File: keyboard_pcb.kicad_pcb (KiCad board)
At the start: 2 copper layers, 436.2 x 123.8 mm, 214 parts, among them J1 Conn_01x04_Female, J2 , J3 Conn_01x03_Male, SW1 SW_Push, SW10 SW_Push, SW100 SW_Push, SW101 SW_Push, SW102 SW_Push, SW103 SW_Push, SW104 SW_Push, SW105 SW_Push, SW11 SW_Push, SW12 SW_Push, SW13 SW_Push, SW14 SW_Push, SW15 SW_Push, SW16 SW_Push, SW17 SW_Push, SW18 SW_Push, SW19 SW_Push, SW2 SW_Push, SW20 SW_Push, SW21 SW_Push, SW22 SW_Push, SW23 SW_Push, SW24 SW_Push, SW25 SW_Push, SW26 SW_Push, SW27 SW_Push, SW28 SW_Push, SW29 SW_Push, SW3 SW_Push, SW30 SW_Push, SW31 SW_Push, SW32 SW_Push, SW33 SW_Push, SW34 SW_Push, SW35 SW_Push, SW36 SW_Push, SW37 SW_Push, SW38 SW_Push, SW39 SW_Push, SW4 SW_Push, SW40 SW_Push, SW41 SW_Push, SW42 SW_Push, SW43 SW_Push, SW44 SW_Push, SW45 SW_Push, SW46 SW_Push, SW47 SW_Push, SW48 SW_Push, SW49 SW_Push, SW5 SW_Push, SW50 SW_Push, SW51 SW_Push, SW52 SW_Push, SW53 SW_Push, SW54 SW_Push, SW55 SW_Push, SW56 SW_Push, SW57 SW_Push, SW58 SW_Push, SW59 SW_Push, SW6 SW_Push, SW60 SW_Push, SW61 SW_Push, SW62 SW_Push, SW63 SW_Push, SW64 SW_Push, SW65 SW_Push, SW66 SW_Push, SW67 SW_Push, SW68 SW_Push, SW69 SW_Push, SW7 SW_Push, SW70 SW_Push, SW71 SW_Push, SW72 SW_Push, SW73 SW_Push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

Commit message: Fixed missing connections and schematic changes
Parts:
- added J4: Conn_01x04_Female, Connector_PinHeader_2.54mm:PinHeader_1x04_P2.54mm_Vertical, F.Cu at (407.0, 19.7)
- moved J3 7.18 mm to (414.7, 14.6), turned to 180 degrees
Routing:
- net ROW4: track 243.8 -> 460.5 mm
- net SDA: track 25.2 -> 39.9 mm
- net 3V3: track 23.7 -> 9.72 mm
- net SCL: track 20.4 -> 32.7 mm
- net 5V: track 36.4 -> 38.5 mm
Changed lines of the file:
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@@
     (thickness 1.6)
     (drawings 8)
-    (tracks 454)
+    (tracks 458)
     (zones 0)
-    (modules 214)
+    (modules 215)
     (nets 146)
   )
@@
     (add_net GND)
   )
+  (module Connector_PinHeader_2.54mm:PinHeader_1x04_P2.54mm_Vertical (layer Front)
+    (at 407.035 19.685 90)
+    (descr "Through hole straight pin header, 1x04, 2.54mm pitch, single row")
+    (tags "Through hole pin header THT 1x04 2.54mm single row")
+    (fp_text reference J4 (at 0 -2.33 90) (layer F.SilkS)
+      (effects (font (size 1 1) (thickness 0.15)))
+    )
+    (fp_text value Conn_01x04_Female (at 0 9.95 90) (layer F.Fab)
+      (effects (font (size 1 1) (thickness 0.15)))
+    )
+    (fp_text user %R (at 0 3.81) (layer F.Fab)
+      (effects (font (size 1 1) (thickness 0.15)))
+    )
+    (fp_line (start -0.635 -1.27) (end 1.27 -1.27) (layer F.Fab) (width 0.1))
+    (fp_line (start 1.27 -1.27) (end 1.27 8.89) (layer F.Fab) (width 0.1))
+    (fp_line (start 1.27 8.89) (end -1.27 8.89) (layer F.Fab) (width 0.1))
+    (fp_line (start -1.27 8.89) (end -1.27 -0.635) (layer F.Fab) (width 0.1))
+    (fp_line (start -1.27 -0.635) (end -0.635 -1.27) (layer F.Fab) (width 0.1))
+    (fp_line (start -1.33 8.95) (end 1.33 8.95) (layer F.SilkS) (width 0.12))
+    (fp_line (start -1.33 1.27) (end -1.33 8.95) (layer F.SilkS) (width 0.12))
+    (fp_line (start 1.33 1.27) (end 1.33 8.95) (layer F.SilkS) (width 0.12))
+    (fp_line (start -1.33 1.27) (end 1.33 1.27) (layer F.SilkS) (width 0.12))
+    (fp_line (start -1.33 0) (end -1.33 -1.33) (layer F.SilkS) (width 0.12))
+    (fp_line (start -1.33 -1.33) (end 0 -1.33) (layer F.SilkS) (width 0.12))
+    (fp_line (start -1.8 -1.8) (end -1.8 9.4) (layer F.CrtYd) (width 0.05))
+    (fp_line (start -1.8 9.4) (end 1.8 9.4) (layer F.CrtYd) (width 0.05))
+    (fp_line (start 1.8 9.4) (end 1.8 -1.8) (layer F.CrtYd) (width 0.05))
+    (fp_line (start 1.8 -1.8) (end -1.8 -1.8) (layer F.CrtYd) (width 0.05))
+    (pad 4 thru_hole oval (at 0 7.62 90) (size 1.7 1.7) (drill 1) (layers *.Cu *.Mask)
+      (net 138 3V3))
+    (pad 3 thru_hole oval (at 0 5.08 90) (size 1.7 1.7) (drill 1) (layers *.Cu *.Mask)
+      (net 145 SDA))
+    (pad 2 thru_hole oval (at 0 2.54 90) (size 1.7 1.7) (drill 1) (layers *.Cu *.Mask)
+      (net 144 SCL))
+    (pad 1 thru_hole rect (at 0 0 90) (size 1.7 1.7) (drill 1) (layers *.Cu *.Mask)
+      (net 1 GND))
+    (model ${KISYS3DMOD}/Connector_PinHeader_2.54mm.3dshapes/PinHeader_1x04_P2.54mm_Vertical.wrl
+      (at (xyz 0 0 0))
+      (scale (xyz 1 1 1))
+      (rotate (xyz 0 0 0))
+    )
+  )
   (module Diode_THT:D_DO-35_SOD27_P7.62mm_Horizontal (layer Front)
     (at 378.46 112.395 90)
@@
   )
   (module Connector_PinHeader_2.54mm:PinHeader_1x03_P2.54mm_Vertical (layer Front)
-    (at 409.575 19.685 90)
+    (at 414.655 14.605 180)
     (descr "Through hole straight pin header, 1x03, 2.54mm pitch, single row")
     (tags "Through hole pin header THT 1x03 2.54mm single row")
-    (fp_text reference J3 (at 0 -2.33 90) (layer F.SilkS)
+    (fp_text reference J3 (at 0 -2.33) (layer F.SilkS)
       (effects (font (size 1 1) (thickness 0.15)))
     )
-    (fp_text value Conn_01x03_Male (at 0 7.41 90) (layer F.Fab)
+    (fp_text value Conn_01x03_Male (at 0 7.41) (layer F.Fab)
       (effects (font (size 1 1) (thickness 0.15)))
     )
@@
     (fp_line (start 1.27 -1.27) (end 1.27 6.35) (layer F.Fab) (width 0.1))
     (fp_line (start -0.635 -1.27) (end 1.27 -1.27) (layer F.Fab) (width 0.1))
-    (fp_text user %R (at 0 2.54) (layer F.Fab)
+    (fp_text user %R (at 0 2.54 90) (layer F.Fab)
       (effects (font (size 1 1) (thickness 0.15)))
     )
-    (pad 3 thru_hole oval (at 0 5.08 90) (size 1.7 1.7) (drill 1) (layers *.Cu *.Mask)
+    (pad 3 thru_hole oval (at 0 5.08 180) (size 1.7 1.7) (drill 1) (layers *.Cu *.Mask)
       (net 135 5V))
-    (pad 2 thru_hole oval (at 0 2.54 90) (size 1.7 1.7) (drill 1) (layers *.Cu *.Mask)
+    (pad 2 thru_hole oval (at 0 2.54 180) (size 1.7 1.7) (drill 1) (layers *.Cu *.Mask)
       (net 138 3V3))
-    (pad 1 thru_hole rect (at 0 0 90) (size 1.7 1.7) (drill 1) (layers *.Cu *.Mask)
+    (pad 1 thru_hole rect (at 0 0 180) (size 1.7 1.7) (drill 1) (layers *.Cu *.Mask)
       (net 1 GND))
     (model ${KISYS3DMOD}/Connector_PinHeader_2.54mm.3dshapes/PinHeader_1x03_P2.54mm_Vertical.wrl
@@
   (segment (start 359.41 74.93) (end 359.41 74.295) (width 0.254) (layer Front) (net 15))
   (segment (start 352.425 81.915) (end 359.41 74.93) (width 0.254) (layer Front) (net 15))
+  (segment (start 230.822 74.295) (end 14.1288 74.295) (width 0.254) (layer Front) (net 15))
   (segment (start 11.7475 55.245) (end 245.11 55.245) (width 0.254) (layer Front) (net 16))
   (segment (start 380.365 19.685) (end 380.365 22.86) (width 0.254) (layer Back) (net 16))
@@
   (segment (start 390.525 104.775) (end 378.46 104.775) (width 0.254) (layer Front) (net 132))
   (segment (start 398.145 95.25) (end 409.575 95.25) (width 0.254) (layer Front) (net 133))
-  (segment (start 395.605 19.685) (end 398.145 22.225) (width 0.381) (layer Front) (net 135))
-  (segment (start 412.115 22.225) (end 414.655 19.685) (width 0.381) (layer Front) (net 135))
-  (segment (start 398.145 22.225) (end 412.115 22.225) (width 0.381) (layer Front) (net 135))
-  (segment (start 414.655 4.445) (end 414.655 19.685) (width 0.381) (layer Front) (net 135))
+  (segment (start 414.655 4.445) (end 414.655 9.525) (width 0.381) (layer Front) (net 135))
+  (segment (start 415.250441 20.925501) (end 417.195 18.980942) (width 0.381) (layer Back) (net 135))
+  (segment (start 396.845501 20.925501) (end 415.250441 20.925501) (width 0.381) (layer Back) (net 135))
+  (segment (start 395.605 19.685) (end 396.845501 20.925501) (width 0.381) (layer Back) (net 135))
+  (segment (start 417.195 12.065) (end 414.655 9.525) (width 0.381) (layer Back) (net 135))
+  (segment (start 417.195 18.980942) (end 417.195 12.065) (width 0.381) (layer Back) (net 135))
   (segment (start 409.985121 6.574879) (end 412.115 4.445) (width 0.4) (layer Front) (net 136))
   (segment (start 404.205 12.355) (end 409.985121 6.574879) (width 0.4) (layer Front) (net 136))
@@
   (segment (start 395.610001 10.795) (end 396.590001 11.775) (width 0.4) (layer Front) (net 137))
   (segment (start 394.335 10.795) (end 395.610001 10.795) (width 0.4) (layer Front) (net 137))
-  (segment (start 390.525 19.685) (end 393.065 22.225) (width 0.381) (layer Back) (net 138))
-  (segment (start 409.575 22.225) (end 412.115 19.685) (width 0.381) (layer Back) (net 138))
-  (segment (start 393.065 22.225) (end 409.575 22.225) (width 0.381) (layer Back) (net 138))
+  (segment (start 417.195 14.605) (end 414.655 12.065) (width 0.381) (layer Front) (net 138))
+  (segment (start 417.195 17.145) (end 417.195 14.605) (width 0.381) (layer Front) (net 138))
+  (segment (start 414.655 19.685) (end 417.195 17.145) (width 0.381) (layer Front) (net 138))
   (segment (start 378.952001 18.557999) (end 397.017999 18.557999) (width 0.254) (layer Front) (net 144))
   (segment (start 377.825 19.685) (end 378.952001 18.557999) (width 0.254) (layer Front) (net 144))
-  (segment (start 397.017999 18.557999) (end 397.51 19.05) (width 0.254) (layer Front) (net 144))
-  (segment (start 395.120065 16.017999) (end 397.206056 18.10399) (width 0.254) (layer Front) (net 145))
-  (segment (start 378.952001 16.017999) (end 395.120065 16.017999) (width 0.254) (layer Front) (net 145))
+  (segment (start 408.397999 18.507999) (end 409.575 19.685) (width 0.254) (layer Front) (net 144))
+  (segment (start 397.067999 18.507999) (end 408.397999 18.507999) (width 0.254) (layer Front) (net 144))
+  (segment (start 397.017999 18.557999) (end 397.067999 18.507999) (width 0.254) (layer Front) (net 144))
+  (segment (start 408.447999 16.017999) (end 412.115 19.685) (width 0.254) (layer Front) (net 145))
+  (segment (start 378.952001 16.017999) (end 408.447999 16.017999) (width 0.254) (layer Front) (net 145))
   (segment (start 375.285 19.685) (end 378.952001 16.017999) (width 0.254) (layer Front) (net 145))
-  (segment (start 397.206056 18.10399) (end 397.831033 18.728967) (width 0.254) (layer Front) (net 145))
   (zone (net 1) (net_name GND) (layer Front) (hatch edge 0.508)
     (connect_pads (clearance 0.508))

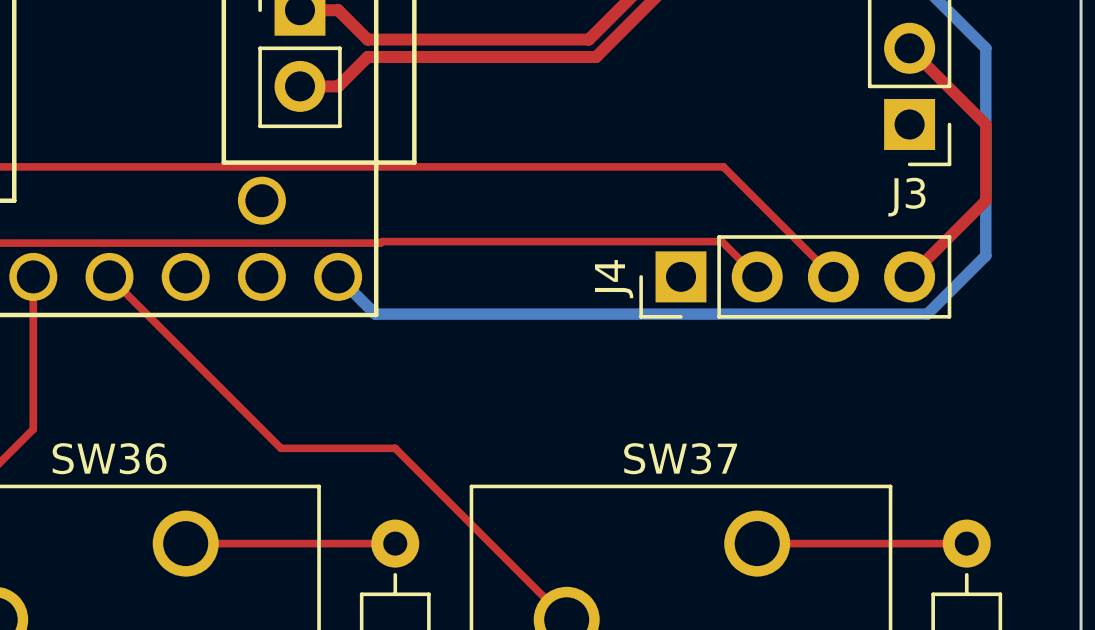
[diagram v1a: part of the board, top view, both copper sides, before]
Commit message: Add 3V3 connection
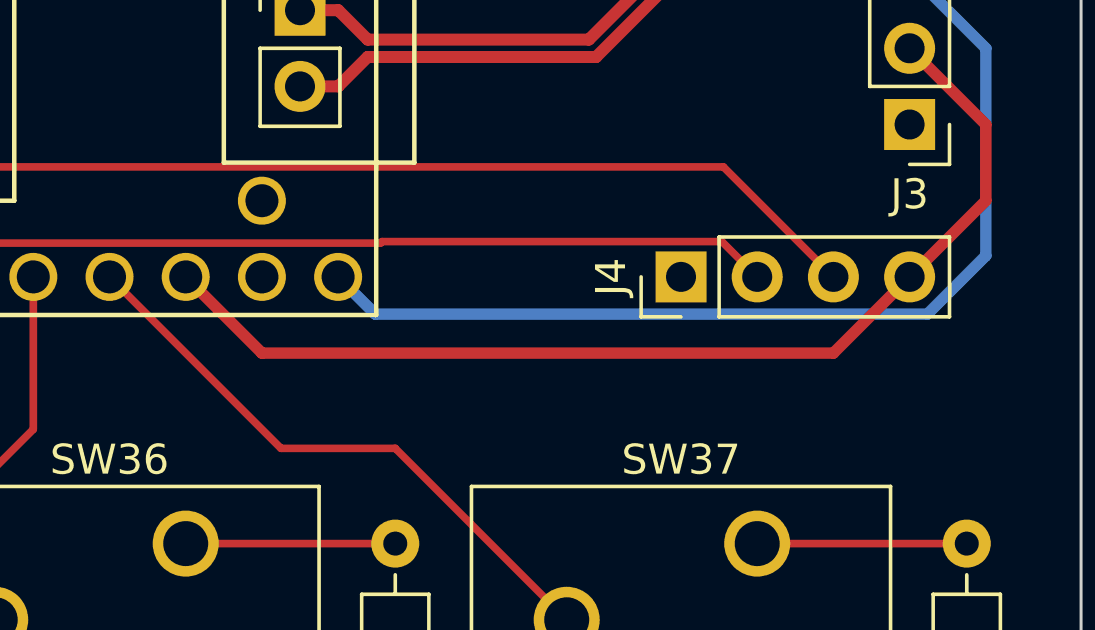
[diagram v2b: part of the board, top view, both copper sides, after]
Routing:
- net 3V3: track 9.72 -> 36.0 mm
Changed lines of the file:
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@@
     (thickness 1.6)
     (drawings 8)
-    (tracks 458)
+    (tracks 461)
     (zones 0)
     (modules 215)
@@
   (segment (start 417.195 17.145) (end 417.195 14.605) (width 0.381) (layer Front) (net 138))
   (segment (start 414.655 19.685) (end 417.195 17.145) (width 0.381) (layer Front) (net 138))
+  (segment (start 390.525 19.685) (end 393.065 22.225) (width 0.381) (layer Front) (net 138))
+  (segment (start 412.115 22.225) (end 414.655 19.685) (width 0.381) (layer Front) (net 138))
+  (segment (start 393.065 22.225) (end 412.115 22.225) (width 0.381) (layer Front) (net 138))
   (segment (start 378.952001 18.557999) (end 397.017999 18.557999) (width 0.254) (layer Front) (net 144))
   (segment (start 377.825 19.685) (end 378.952001 18.557999) (width 0.254) (layer Front) (net 144))

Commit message: Split some traces
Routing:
- net ROW3: track 441.0 -> 438.8 mm
- net ROW1: track 367.4 -> 366.8 mm
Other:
- net class USB added: clearance 0.18, trace_width 0.254, via_dia 0.8, via_drill 0.4
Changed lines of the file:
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@@
     (thickness 1.6)
     (drawings 8)
-    (tracks 461)
+    (tracks 514)
     (zones 0)
     (modules 215)
@@
     (add_net COL8)
     (add_net COL9)
-    (add_net D+)
-    (add_net D-)
     (add_net "Net-(D1-Pad2)")
     (add_net "Net-(D10-Pad2)")
@@
     (add_net GND)
   )
+  (net_class USB ""
+    (clearance 0.18)
+    (trace_width 0.254)
+    (via_dia 0.8)
+    (via_drill 0.4)
+    (uvia_dia 0.3)
+    (uvia_drill 0.1)
+    (diff_pair_width 0.4)
+    (diff_pair_gap 0.18)
+    (add_net D+)
+    (add_net D-)
+  )
   (module Connector_PinHeader_2.54mm:PinHeader_1x04_P2.54mm_Vertical (layer Front)
     (at 407.035 19.685 90)
@@
   (gr_line (start -15.875 121.285) (end -15.875 2.54) (layer Edge.Cuts) (width 0.1))
   (gr_line (start 417.83 123.825) (end -13.335 123.825) (layer Edge.Cuts) (width 0.1))
-  (segment (start 6.985 17.145) (end 335.598 17.145) (width 0.254) (layer Front) (net 2))
   (segment (start 349.885 17.145) (end 335.598 17.145) (width 0.254) (layer Front) (net 2))
   (segment (start 370.205 6.985) (end 368.935 8.255) (width 0.254) (layer Front) (net 2))
@@
   (segment (start 360.045 8.255) (end 351.155 17.145) (width 0.254) (layer Front) (net 2))
   (segment (start 351.155 17.145) (end 349.885 17.145) (width 0.254) (layer Front) (net 2))
+  (segment (start 6.985 17.145) (end 45.085 17.145) (width 0.254) (layer Front) (net 2))
+  (segment (start 45.085 17.145) (end 64.135 17.145) (width 0.254) (layer Front) (net 2))
+  (segment (start 64.135 17.145) (end 82.55 17.145) (width 0.254) (layer Front) (net 2))
+  (segment (start 83.185 17.145) (end 102.235 17.145) (width 0.254) (layer Front) (net 2))
+  (segment (start 102.235 17.145) (end 130.81 17.145) (width 0.254) (layer Front) (net 2))
+  (segment (start 130.81 17.145) (end 149.86 17.145) (width 0.254) (layer Front) (net 2))
+  (segment (start 149.86 17.145) (end 168.91 17.145) (width 0.254) (layer Front) (net 2))
+  (segment (start 168.91 17.145) (end 187.96 17.145) (width 0.254) (layer Front) (net 2))
+  (segment (start 187.96 17.145) (end 216.535 17.145) (width 0.254) (layer Front) (net 2))
+  (segment (start 216.535 17.145) (end 235.585 17.145) (width 0.254) (layer Front) (net 2))
+  (segment (start 235.585 17.145) (end 254.635 17.145) (width 0.254) (layer Front) (net 2))
+  (segment (start 254.635 17.145) (end 273.685 17.145) (width 0.254) (layer Front) (net 2))
+  (segment (start 273.685 17.145) (end 297.498 17.145) (width 0.254) (layer Front) (net 2))
+  (segment (start 297.498 17.145) (end 316.548 17.145) (width 0.254) (layer Front) (net 2))
+  (segment (start 316.548 17.145) (end 335.598 17.145) (width 0.254) (layer Front) (net 2))
   (segment (start 403.225 62.701962) (end 403.225 97.79) (width 0.254) (layer Back) (net 3))
   (segment (start 403.225 31.115) (end 403.225 62.701962) (width 0.254) (layer Back) (net 3))
@@
   (segment (start 359.41 74.93) (end 359.41 74.295) (width 0.254) (layer Front) (net 15))
   (segment (start 352.425 81.915) (end 359.41 74.93) (width 0.254) (layer Front) (net 15))
-  (segment (start 230.822 74.295) (end 14.1288 74.295) (width 0.254) (layer Front) (net 15))
-  (segment (start 11.7475 55.245) (end 245.11 55.245) (width 0.254) (layer Front) (net 16))
+  (segment (start 14.1288 74.295) (end 40.3225 74.295) (width 0.254) (layer Front) (net 15))
+  (segment (start 40.3225 74.295) (end 59.3725 74.295) (width 0.254) (layer Front) (net 15))
+  (segment (start 59.3725 74.295) (end 78.4225 74.295) (width 0.254) (layer Front) (net 15))
+  (segment (start 78.4225 74.295) (end 97.4725 74.295) (width 0.254) (layer Front) (net 15))
+  (segment (start 97.4725 74.295) (end 116.522 74.295) (width 0.254) (layer Front) (net 15))
+  (segment (start 116.522 74.295) (end 135.572 74.295) (width 0.254) (layer Front) (net 15))
+  (segment (start 135.572 74.295) (end 154.622 74.295) (width 0.254) (layer Front) (net 15))
+  (segment (start 154.622 74.295) (end 173.672 74.295) (width 0.254) (layer Front) (net 15))
+  (segment (start 173.672 74.295) (end 192.722 74.295) (width 0.254) (layer Front) (net 15))
+  (segment (start 192.722 74.295) (end 211.772 74.295) (width 0.254) (layer Front) (net 15))
+  (segment (start 211.772 74.295) (end 230.822 74.295) (width 0.254) (layer Front) (net 15))
   (segment (start 380.365 19.685) (end 380.365 22.86) (width 0.254) (layer Back) (net 16))
   (segment (start 380.365 22.86) (end 376.555 26.67) (width 0.254) (layer Back) (net 16))
@@
   (segment (start 252.095 64.77) (end 287.973 64.77) (width 0.254) (layer Front) (net 16))
   (segment (start 288.1315 64.6115) (end 297.498 55.245) (width 0.254) (layer Front) (net 16))
-  (segment (start 377.19 55.245) (end 297.498 55.245) (width 0.254) (layer Front) (net 16))
-  (segment (start 380.365 55.245) (end 377.19 55.245) (width 0.254) (layer Front) (net 16))
-  (segment (start 382.905 57.785) (end 380.365 55.245) (width 0.254) (layer Front) (net 16))
-  (segment (start 384.175 64.77) (end 382.905 63.5) (width 0.254) (layer Front) (net 16))
-  (segment (start 382.905 63.5) (end 382.905 57.785) (width 0.254) (layer Front) (net 16))
-  (segment (start 398.145 64.77) (end 384.175 64.77) (width 0.254) (layer Front) (net 16))
-  (segment (start 395.605 36.195) (end 416.56 36.195) (width 0.254) (layer Front) (net 17))
-  (segment (start 385.445 36.195) (end 395.605 36.195) (width 0.254) (layer Front) (net 17))
+  (segment (start 11.7475 55.245) (end 35.56 55.245) (width 0.254) (layer Front) (net 16))
+  (segment (start 35.56 55.245) (end 54.61 55.245) (width 0.254) (layer Front) (net 16))
+  (segment (start 54.61 55.245) (end 73.66 55.245) (width 0.254) (layer Front) (net 16))
+  (segment (start 73.66 55.245) (end 92.71 55.245) (width 0.254) (layer Front) (net 16))
+  (segment (start 92.71 55.245) (end 111.76 55.245) (width 0.254) (layer Front) (net 16))
+  (segment (start 111.76 55.245) (end 130.81 55.245) (width 0.254) (layer Front) (net 16))
+  (segment (start 130.81 55.245) (end 149.86 55.245) (width 0.254) (layer Front) (net 16))
+  (segment (start 149.86 55.245) (end 168.91 55.245) (width 0.254) (layer Front) (net 16))
+  (segment (start 168.91 55.245) (end 187.96 55.245) (width 0.254) (layer Front) (net 16))
+  (segment (start 187.96 55.245) (end 207.01 55.245) (width 0.254) (layer Front) (net 16))
+  (segment (start 207.01 55.245) (end 226.06 55.245) (width 0.254) (layer Front) (net 16))
+  (segment (start 226.06 55.245) (end 245.11 55.245) (width 0.254) (layer Front) (net 16))
+  (segment (start 297.498 55.245) (end 316.548 55.245) (width 0.254) (layer Front) (net 16))
+  (segment (start 316.548 55.245) (end 335.598 55.245) (width 0.254) (layer Front) (net 16))
+  (segment (start 335.598 55.245) (end 359.41 55.245) (width 0.254) (layer Front) (net 16))
+  (segment (start 359.41 55.245) (end 378.46 55.245) (width 0.254) (layer Front) (net 16))
+  (segment (start 378.46 57.15) (end 382.905 61.595) (width 0.254) (layer Front) (net 16))
+  (segment (start 378.46 55.245) (end 378.46 57.15) (width 0.254) (layer Front) (net 16))
+  (segment (start 386.08 64.77) (end 398.145 64.77) (width 0.254) (layer Front) (net 16))
+  (segment (start 382.905 61.595) (end 386.08 64.77) (width 0.254) (layer Front) (net 16))
   (segment (start 396.875 36.195) (end 397.51 36.195) (width 0.254) (layer Front) (net 17))
   (segment (start 382.905 19.685) (end 382.905 24.13) (width 0.254) (layer Front) (net 17))
@@
   (segment (start 379.73 36.195) (end 378.46 36.195) (width 0.254) (layer Front) (net 17))
   (segment (start 381 34.925) (end 379.73 36.195) (width 0.254) (layer Front) (net 17))
-  (segment (start 247.65 36.195) (end 385.445 36.195) (width 0.254) (layer Front) (net 17))
-  (segment (start 6.985 36.195) (end 247.65 36.195) (width 0.254) (layer Front) (net 17))
+  (segment (start 397.51 36.195) (end 416.56 36.195) (width 0.254) (layer Front) (net 17))
+  (segment (start 397.51 36.195) (end 378.46 36.195) (width 0.254) (layer Front) (net 17))
+  (segment (start 378.46 36.195) (end 359.41 36.195) (width 0.254) (layer Front) (net 17))
+  (segment (start 359.41 36.195) (end 335.598 36.195) (width 0.254) (layer Front) (net 17))
+  (segment (start 335.598 36.195) (end 316.548 36.195) (width 0.254) (layer Front) (net 17))
+  (segment (start 316.548 36.195) (end 297.498 36.195) (width 0.254) (layer Front) (net 17))
+  (segment (start 297.498 36.195) (end 273.685 36.195) (width 0.254) (layer Front) (net 17))
+  (segment (start 273.685 36.195) (end 235.585 36.195) (width 0.254) (layer Front) (net 17))
+  (segment (start 235.585 36.195) (end 216.535 36.195) (width 0.254) (layer Front) (net 17))
+  (segment (start 216.535 36.195) (end 197.485 36.195) (width 0.254) (layer Front) (net 17))
+  (segment (start 197.485 36.195) (end 178.435 36.195) (width 0.254) (layer Front) (net 17))
+  (segment (start 178.435 36.195) (end 159.385 36.195) (width 0.254) (layer Front) (net 17))
+  (segment (start 159.385 36.195) (end 140.335 36.195) (width 0.254) (layer Front) (net 17))
+  (segment (start 140.335 36.195) (end 121.285 36.195) (width 0.254) (layer Front) (net 17))
+  (segment (start 121.285 36.195) (end 102.235 36.195) (width 0.254) (layer Front) (net 17))
+  (segment (start 102.235 36.195) (end 83.185 36.195) (width 0.254) (layer Front) (net 17))
+  (segment (start 83.185 36.195) (end 64.135 36.195) (width 0.254) (layer Front) (net 17))
+  (segment (start 64.135 36.195) (end 45.085 36.195) (width 0.254) (layer Front) (net 17))
+  (segment (start 45.085 36.195) (end 26.035 36.195) (width 0.254) (layer Front) (net 17))
+  (segment (start 26.035 36.195) (end 6.985 36.195) (width 0.254) (layer Front) (net 17))
   (segment (start 284.162 12.065) (end 284.162 50.165) (width 0.254) (layer Back) (net 18))
   (segment (start 284.162 50.165) (end 284.162 107.315) (width 0.254) (layer Back) (net 18))

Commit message: Put schematic onto one page
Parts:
- J1: value Conn_01x04_Female -> USB
- J3: value Conn_01x03_Male -> Power
- J4: value Conn_01x04_Female -> I2C

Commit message: Migrated to KiCad 6
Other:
- net class Default removed
- net class Power removed
- net class USB removed
